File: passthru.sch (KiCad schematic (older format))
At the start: 2 parts

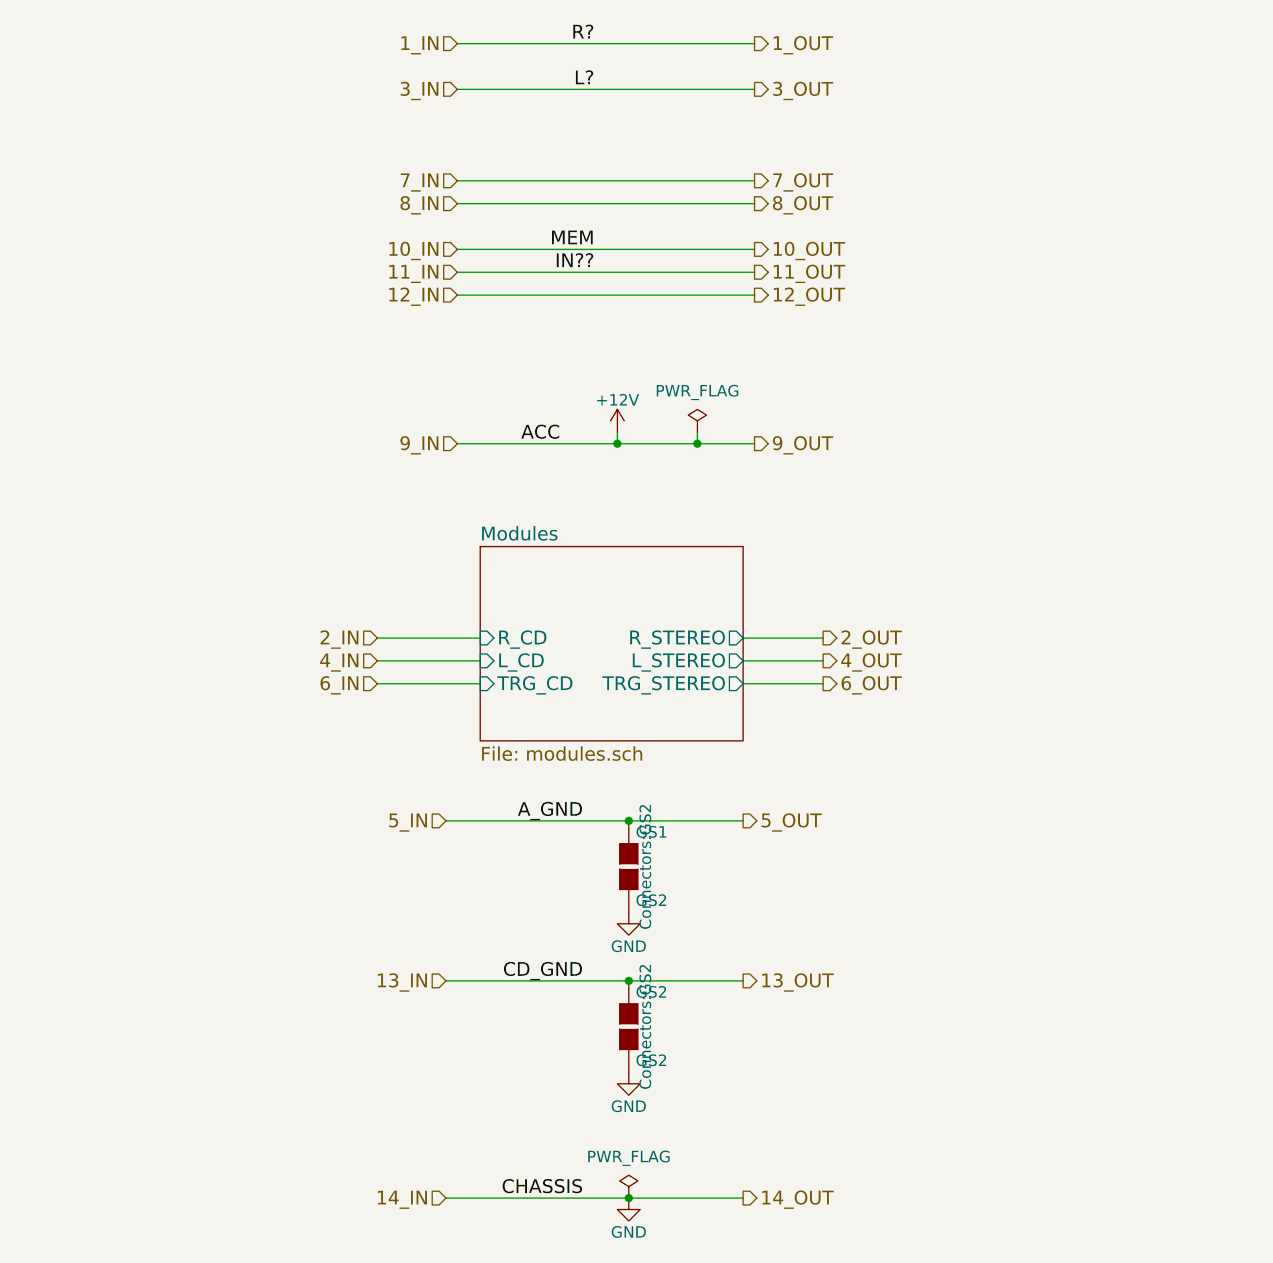
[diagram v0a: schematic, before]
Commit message: Adjust some cap prefixes and add large CD/Stereo labels to top level pages.
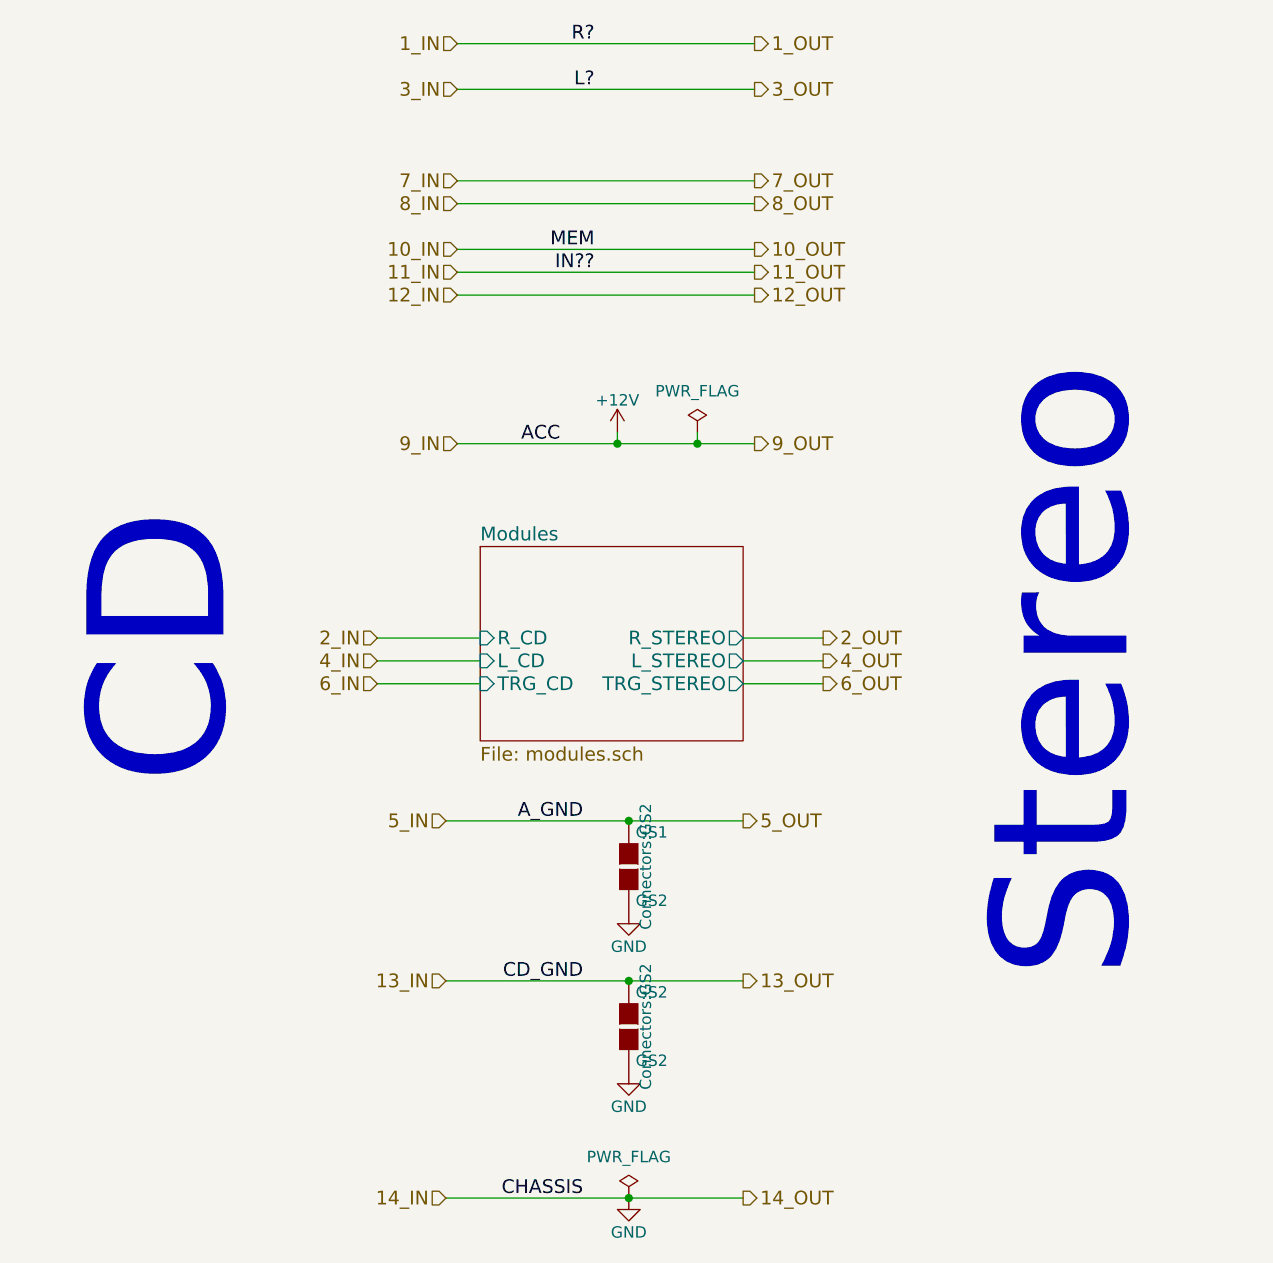
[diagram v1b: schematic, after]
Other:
- note added: "CD"
- note added: "Stereo"
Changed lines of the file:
@@
 	1    0    0    -1
 $EndComp
+Text Notes 3750 4450 1    600  ~ 0
+CD
+Text Notes 7700 5300 1    600  ~ 0
+Stereo
 $EndSCHEMATC

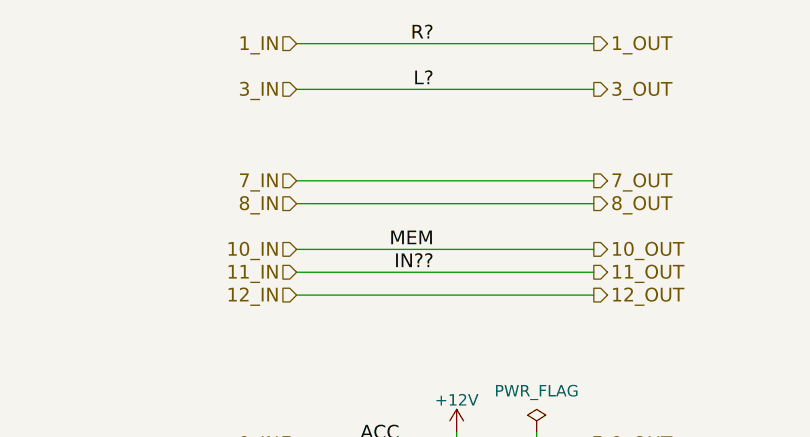
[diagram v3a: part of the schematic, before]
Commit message: Voltage regulator adjustments and tidying
Switch to LD1117 component and add decoupling caps.
Add a decoupling cap to the audio switch
Shift some status LEDs to modules layer
Use ProMini instead of ProMicro
Update BOM
Update netlist
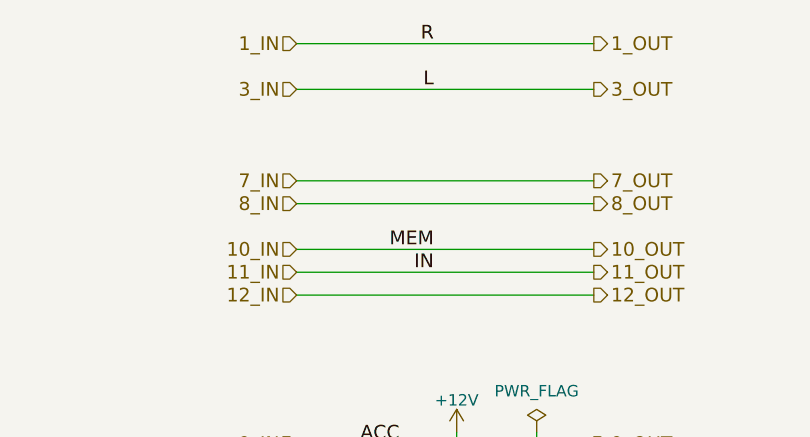
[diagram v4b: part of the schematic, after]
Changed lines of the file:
@@
 14_OUT
 Text Label 5300 1200 2    60   ~ 0
-R?
+R
 Text Label 5300 1400 2    60   ~ 0
-L?
+L
 Text Label 5250 4600 2    60   ~ 0
 A_GND
@@
 MEM
 Text Label 5300 2200 2    60   ~ 0
-IN??
+IN
 Text Label 5250 5300 2    60   ~ 0
 CD_GND

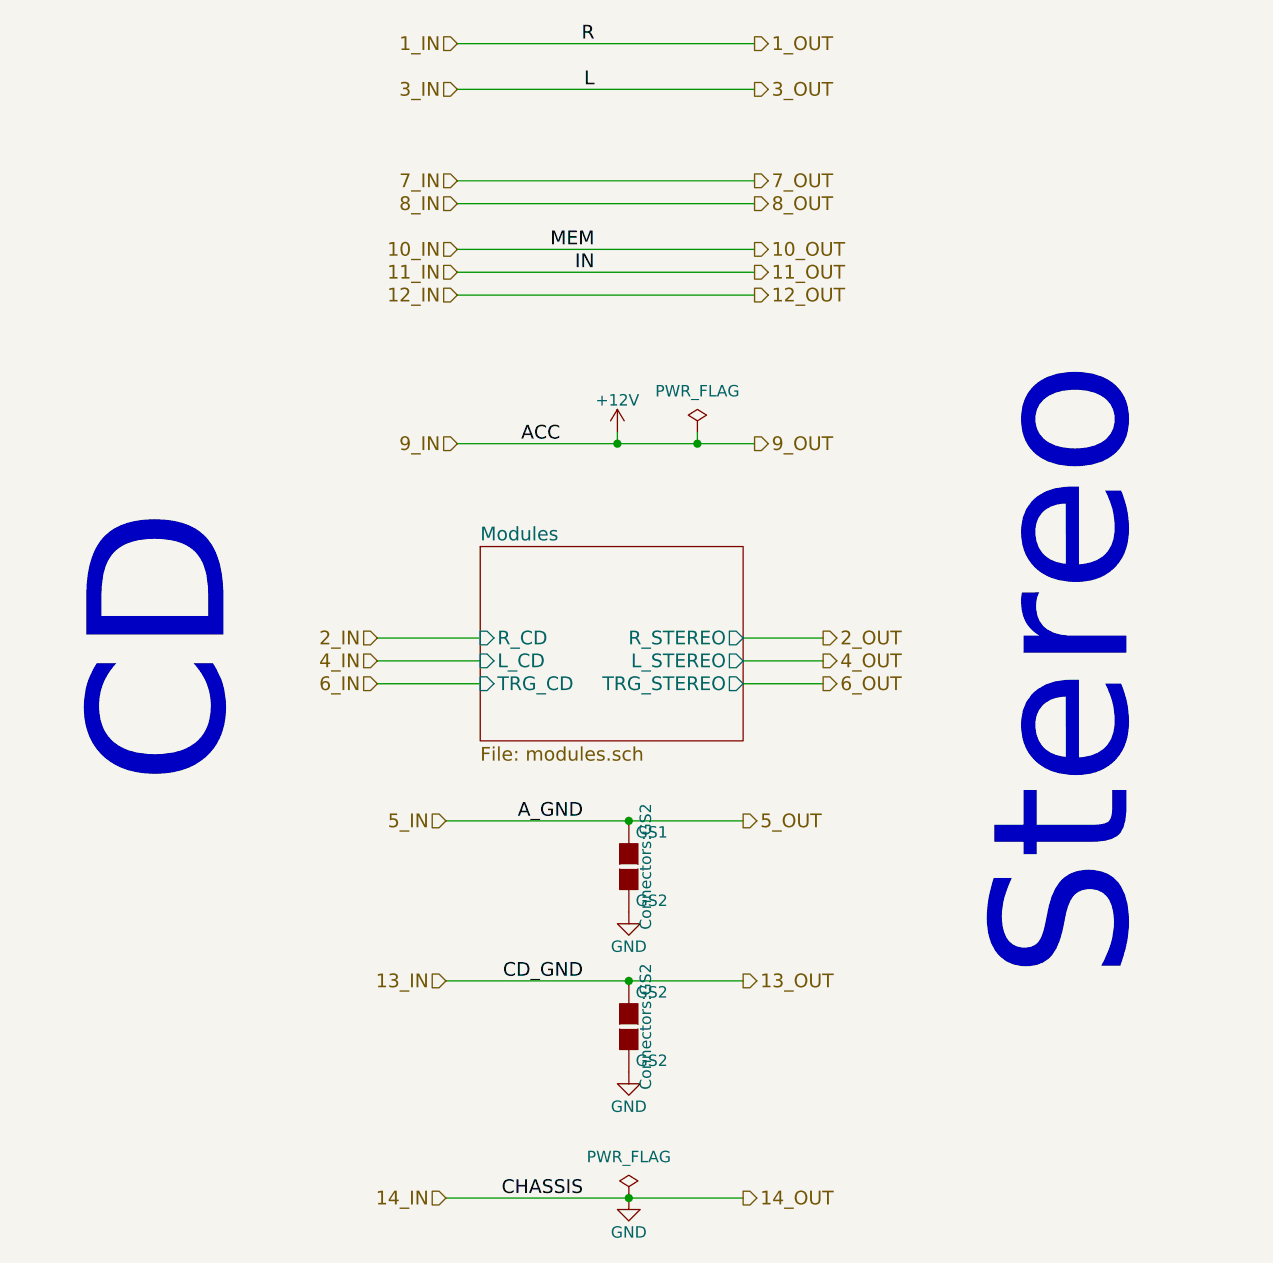
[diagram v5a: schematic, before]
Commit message: Separate audio ground from power ground
The connection between the CD player and stereo has a separate line for
audio ground and the chassis ground. I didn't previously understand why
this was necessary, so I tied them together. They were tied together in
the stereo anyway. The reason is that when using power, there must be
current returning on the ground line, and since that ground line is not
free of resistance, that causes a slight voltage change. That voltage
difference causes a disagreement in what ground is, and at audio levels,
that makes a significant difference. By isolating the audio ground to a
separate wire that doesn't carry current, we keep the ground potential
the same between the devices, and the audio comes out much cleaner.

On the main connector, I've kept the chassis ground as the power ground,
and only connected the audio ground to the mid-rail on the line driver,
and the line-in ground, as those are the places where audio ground
potential will matter.

As I now understand the grounding situation better, I'm removing the
ground jumper pads.

I will also consider removing the voltage regulator if I can get enough
power out of the regulator on board with the MCU.
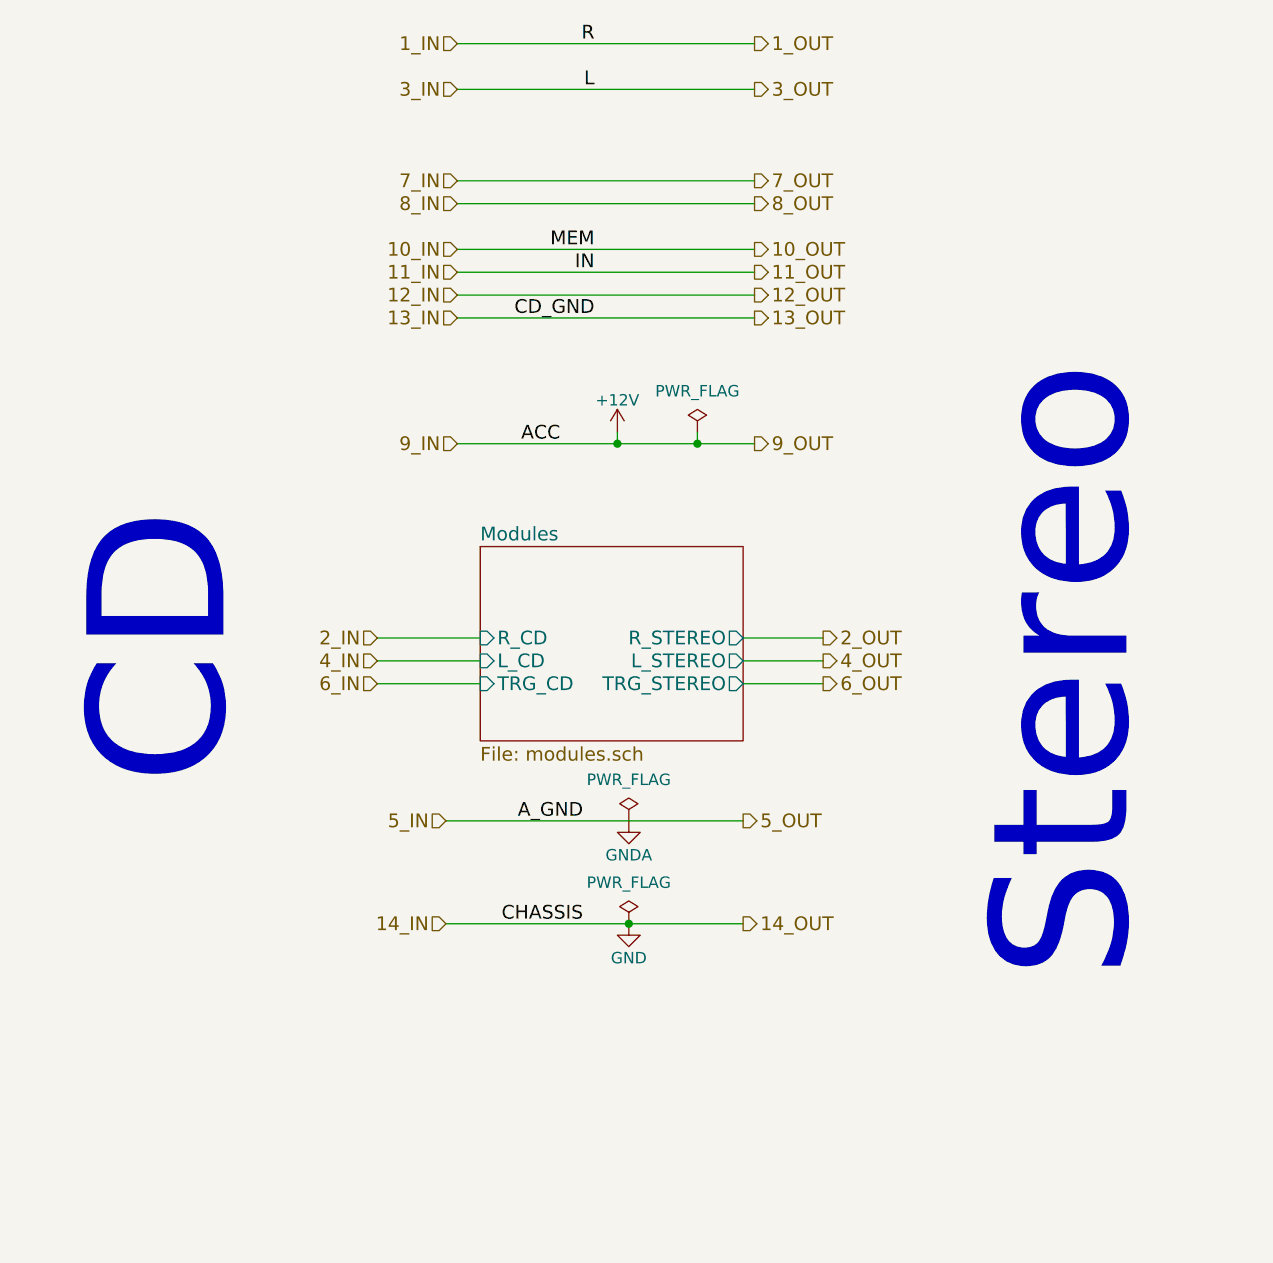
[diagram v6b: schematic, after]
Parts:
- removed GS1, GS2: GS2, Connectors:GS2, symbol GS2
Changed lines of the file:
@@
 	4700 2300 6000 2300
 Wire Wire Line
-	4650 5300 5950 5300
+	4700 2400 6000 2400
 Wire Wire Line
-	4650 6250 5950 6250
+	4650 5050 5950 5050
 Text HLabel 4700 1200 0    60   Input ~ 0
 1_IN
@@
 Text HLabel 4700 2300 0    60   Input ~ 0
 12_IN
-Text HLabel 4650 5300 0    60   Input ~ 0
+Text HLabel 4700 2400 0    60   Input ~ 0
 13_IN
-Text HLabel 4650 6250 0    60   Input ~ 0
+Text HLabel 4650 5050 0    60   Input ~ 0
 14_IN
 Text HLabel 6000 1200 2    60   Output ~ 0
@@
 Text HLabel 6000 2300 2    60   Output ~ 0
 12_OUT
-Text HLabel 5950 5300 2    60   Output ~ 0
+Text HLabel 6000 2400 2    60   Output ~ 0
 13_OUT
-Text HLabel 5950 6250 2    60   Output ~ 0
+Text HLabel 5950 5050 2    60   Output ~ 0
 14_OUT
 Text Label 5300 1200 2    60   ~ 0
@@
 Text Label 5300 2200 2    60   ~ 0
 IN
-Text Label 5250 5300 2    60   ~ 0
+Text Label 5300 2400 2    60   ~ 0
 CD_GND
-Text Label 5250 6250 2    60   ~ 0
+Text Label 5250 5050 2    60   ~ 0
 CHASSIS
 Wire Wire Line
@@
 L GND #PWR01
 U 1 1 58B1285E
-P 5450 6250
-F 0 "#PWR01" H 5450 6000 50  0001 C CNN
-F 1 "GND" H 5450 6100 50  0000 C CNN
-F 2 "" H 5450 6250 50  0000 C CNN
-F 3 "" H 5450 6250 50  0000 C CNN
-	1    5450 6250
+P 5450 5050
+F 0 "#PWR01" H 5450 4800 50  0001 C CNN
+F 1 "GND" H 5450 4900 50  0000 C CNN
+F 2 "" H 5450 5050 50  0000 C CNN
+F 3 "" H 5450 5050 50  0000 C CNN
+	1    5450 5050
 	1    0    0    -1
 $EndComp
-Connection ~ 5450 5300
-Connection ~ 5450 6250
-Connection ~ 5450 4600
+Connection ~ 5450 5050
 $Comp
 L PWR_FLAG #FLG02
@@
 Connection ~ 5400 2950
 $Comp
-L GS2 GS1
-U 1 1 58B4F2F1
-P 5450 4800
-F 0 "GS1" H 5550 4950 50  0000 C CNN
-F 1 "GS2" H 5550 4651 50  0000 C CNN
-F 2 "Connectors:GS2" V 5524 4800 50  0000 C CNN
-F 3 "" H 5450 4800 50  0000 C CNN
-	1    5450 4800
-	1    0    0    -1
-$EndComp
-$Comp
 L PWR_FLAG #FLG04
 U 1 1 58B12B41
-P 5450 6250
-F 0 "#FLG04" H 5450 6345 50  0001 C CNN
-F 1 "PWR_FLAG" H 5450 6430 50  0000 C CNN
-F 2 "" H 5450 6250 50  0000 C CNN
-F 3 "" H 5450 6250 50  0000 C CNN
-	1    5450 6250
-	1    0    0    -1
-$EndComp
-$Comp
-L GND #PWR05
-U 1 1 58B4FAC7
-P 5450 5000
-F 0 "#PWR05" H 5450 4750 50  0001 C CNN
-F 1 "GND" H 5450 4850 50  0000 C CNN
-F 2 "" H 5450 5000 50  0000 C CNN
-F 3 "" H 5450 5000 50  0000 C CNN
-	1    5450 5000
-	1    0    0    -1
-$EndComp
-$Comp
-L GS2 GS2
-U 1 1 58B4FB59
-P 5450 5500
-F 0 "GS2" H 5550 5650 50  0000 C CNN
-F 1 "GS2" H 5550 5351 50  0000 C CNN
-F 2 "Connectors:GS2" V 5524 5500 50  0000 C CNN
-F 3 "" H 5450 5500 50  0000 C CNN
-	1    5450 5500
-	1    0    0    -1
-$EndComp
-$Comp
-L GND #PWR06
-U 1 1 58B4FBCF
-P 5450 5700
-F 0 "#PWR06" H 5450 5450 50  0001 C CNN
-F 1 "GND" H 5450 5550 50  0000 C CNN
-F 2 "" H 5450 5700 50  0000 C CNN
-F 3 "" H 5450 5700 50  0000 C CNN
-	1    5450 5700
+P 5450 5050
+F 0 "#FLG04" H 5450 5145 50  0001 C CNN
+F 1 "PWR_FLAG" H 5450 5230 50  0000 C CNN
+F 2 "" H 5450 5050 50  0000 C CNN
+F 3 "" H 5450 5050 50  0000 C CNN
+	1    5450 5050
 	1    0    0    -1
 $EndComp
@@
 Text Notes 7700 5300 1    600  ~ 0
 Stereo
+$Comp
+L GNDA #PWR05
+U 1 1 59C094BB
+P 5450 4600
+F 0 "#PWR05" H 5450 4350 50  0001 C CNN
+F 1 "GNDA" H 5450 4450 50  0000 C CNN
+F 2 "" H 5450 4600 50  0000 C CNN
+F 3 "" H 5450 4600 50  0000 C CNN
+	1    5450 4600
+	1    0    0    -1
+$EndComp
+$Comp
+L PWR_FLAG #FLG06
+U 1 1 59C09583
+P 5450 4600
+F 0 "#FLG06" H 5450 4695 50  0001 C CNN
+F 1 "PWR_FLAG" H 5450 4780 50  0000 C CNN
+F 2 "" H 5450 4600 50  0000 C CNN
+F 3 "" H 5450 4600 50  0000 C CNN
+	1    5450 4600
+	1    0    0    -1
+$EndComp
 $EndSCHEMATC
